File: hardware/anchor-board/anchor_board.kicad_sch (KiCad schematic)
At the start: 72 parts, among them J1 USB4105-GF-A, J2 SWD 2x5 1.27mm, J3 UART TX/RX/GND, J4 GPIO breakout, J5 3V0 current shunt, J6 LED disable, J7 Reset/boot strap, J8 TC2030 SWD, SW1 SKHHALA010, U1 DWM3001C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

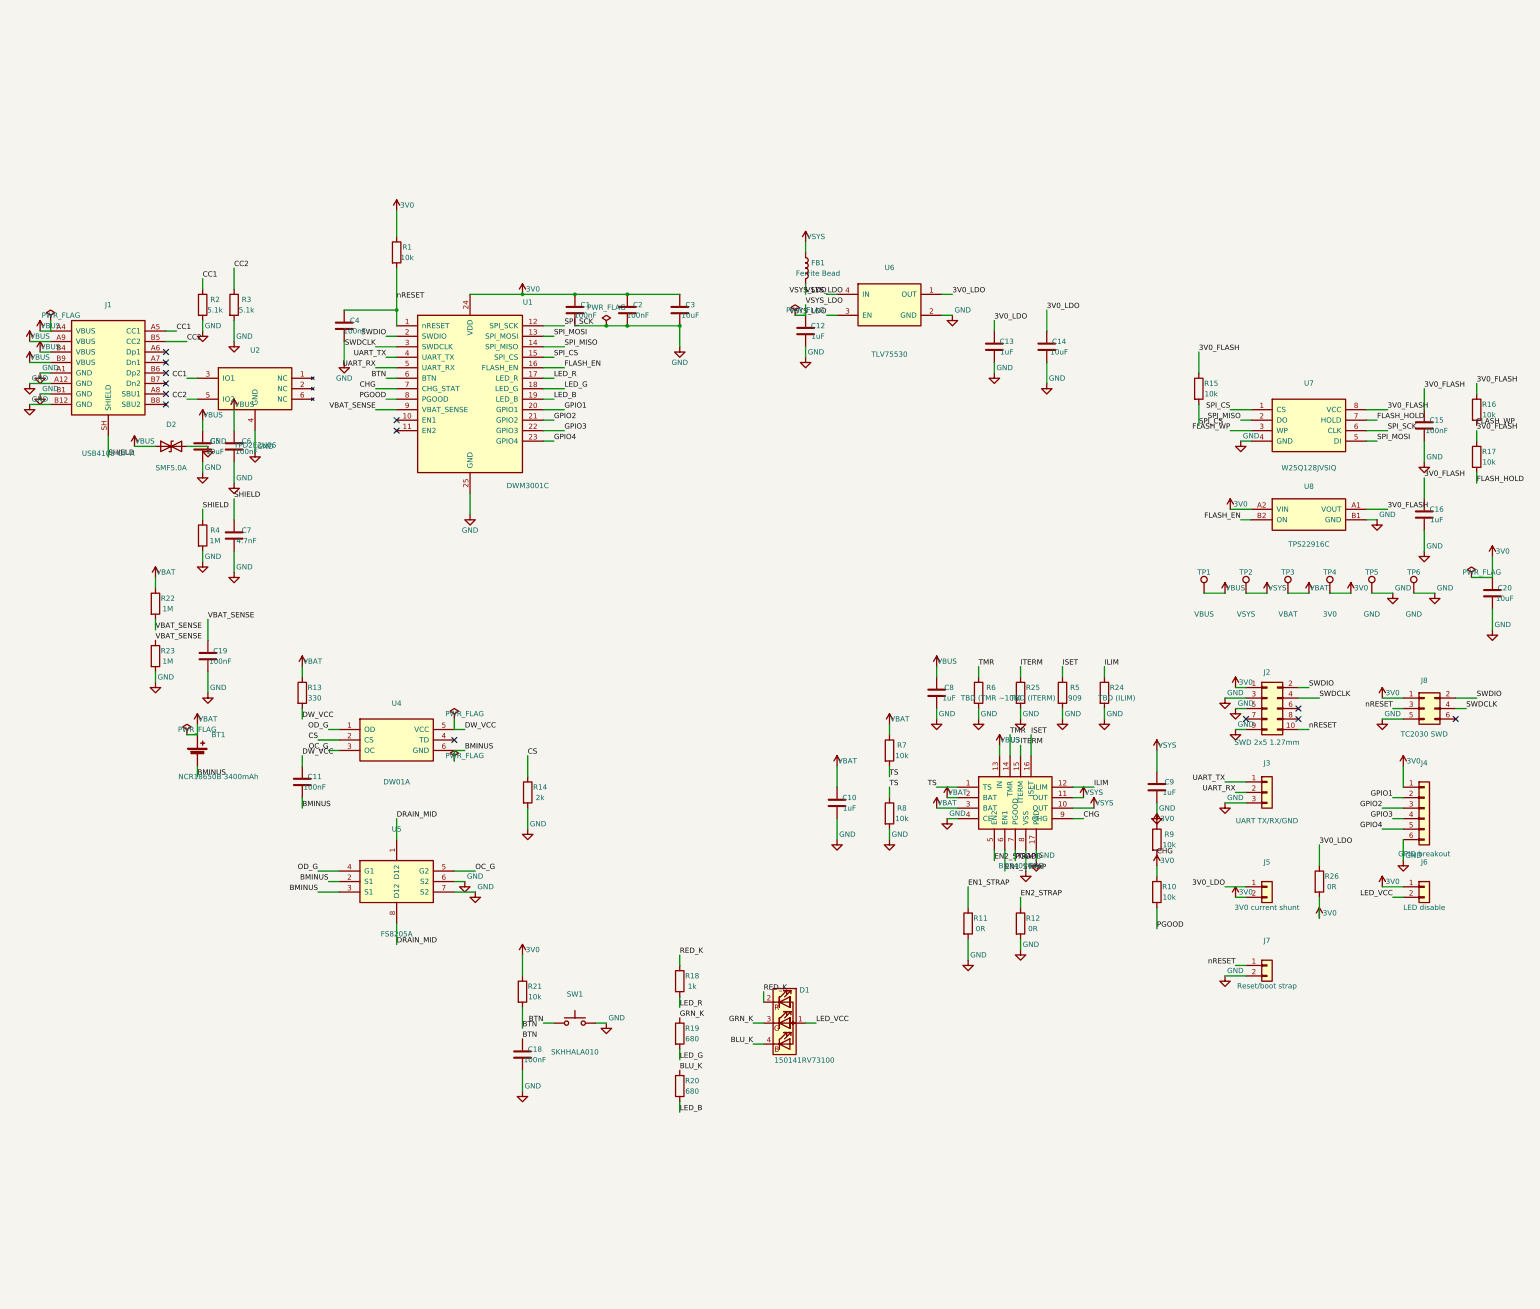
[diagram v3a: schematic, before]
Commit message: Group schematic into framed functional sections
Each block (§4.1-4.9 + §7 dev rail) is now translated as a unit into
its own region of the sheet and wrapped in a dashed frame with a
heading, instead of components being scattered across the page.

- SECTION_REFS maps every ref to its block; SECTION_TARGET gives each
  block a placement on the grid, roughly following power flow (USB-C
  top-left, rails across the top, module centre, peripherals down the
  right, dev aids along the bottom)
- blocks keep their internal relative layout — only the whole block
  moves; §4.1's hand-drawn wires/junctions/ports translate with it
- per-section frames are sized from the actual extent of each block's
  components, stubs and labels (sec_pts), drawn as a dashed polyline
  with a text heading
- ERC still 0/0

Within-block density (e.g. the charger, USB-C) is unchanged and left
for hand-tidying in KiCad.
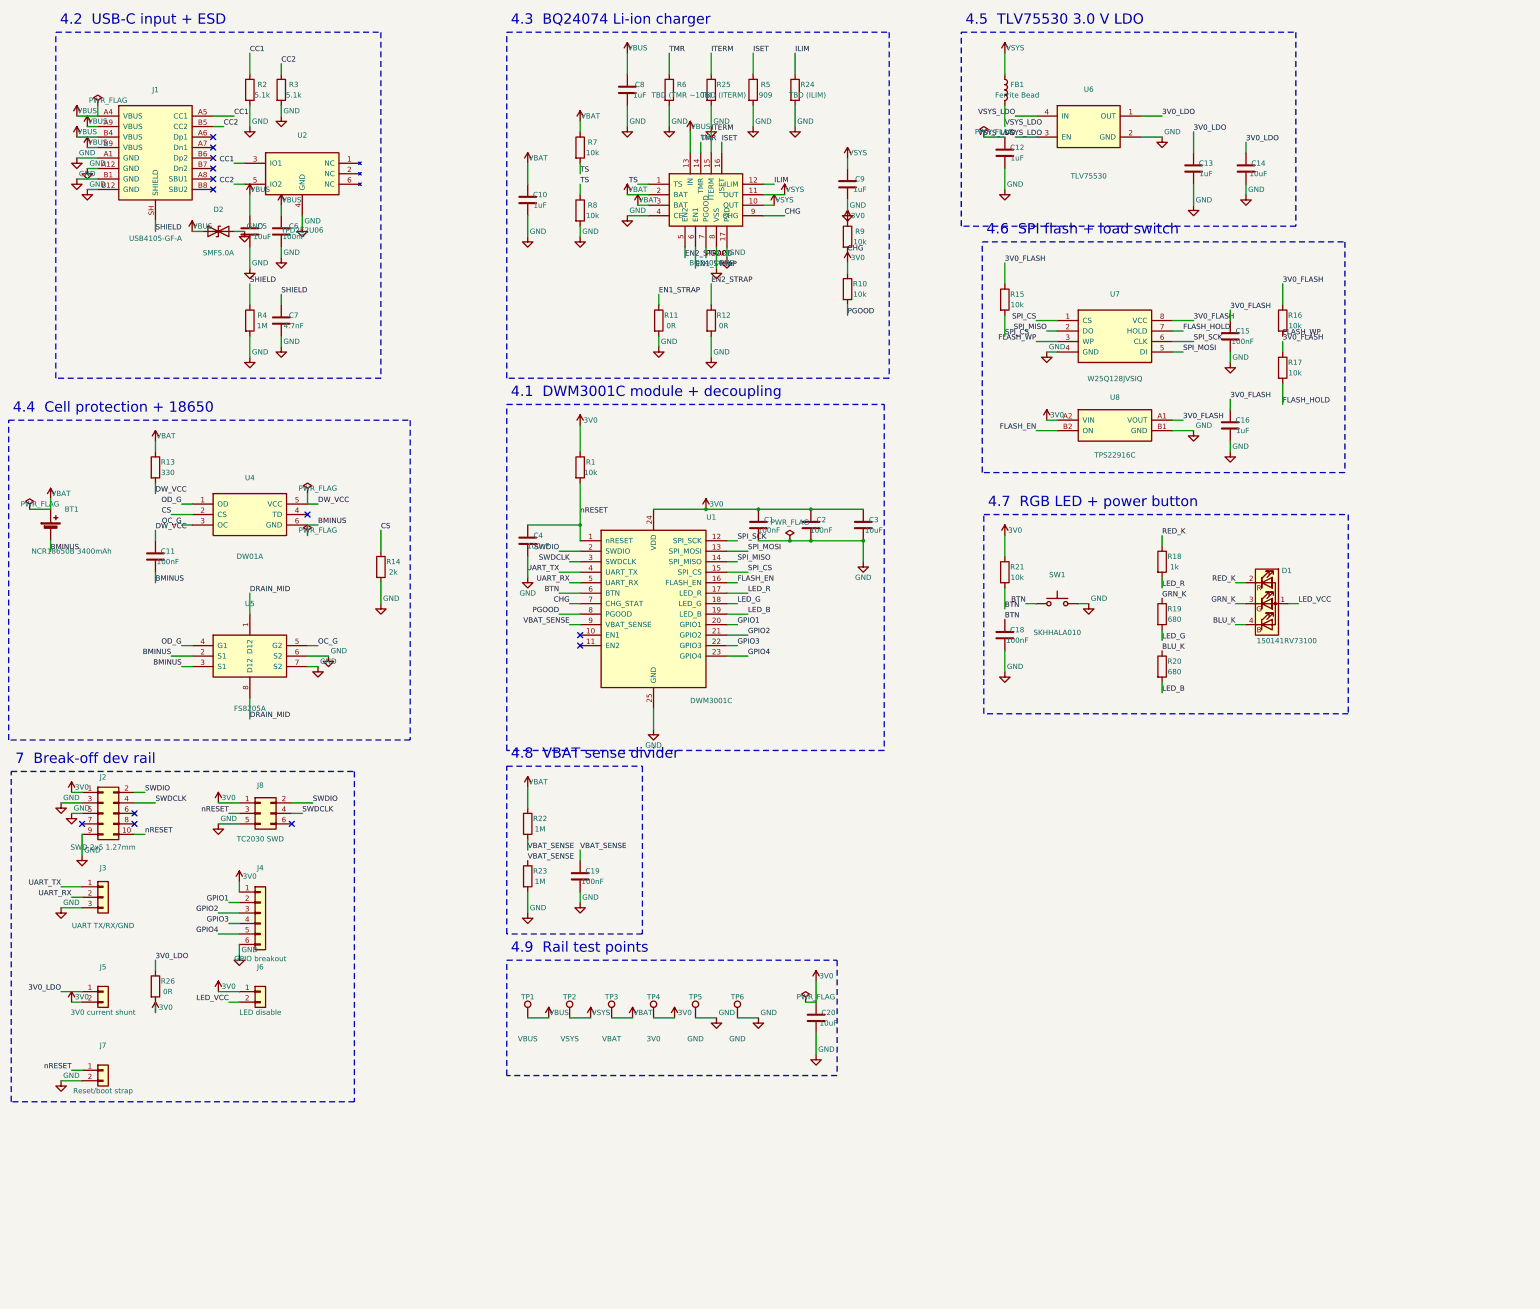
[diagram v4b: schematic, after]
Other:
- note added: "4.1 DWM3001C module + decoupling"
- note added: "4.2 USB-C input + ESD"
- note added: "4.3 BQ24074 Li-ion charger"
- note added: "4.4 Cell protection + 18650"
- note added: "4.5 TLV75530 3.0 V LDO"
- note added: "4.6 SPI flash + load switch"
- note added: "4.7 RGB LED + power button"
- note added: "4.8 VBAT sense divider"
- note added: "4.9 Rail test points"
- note added: "7 Break-off dev rail"

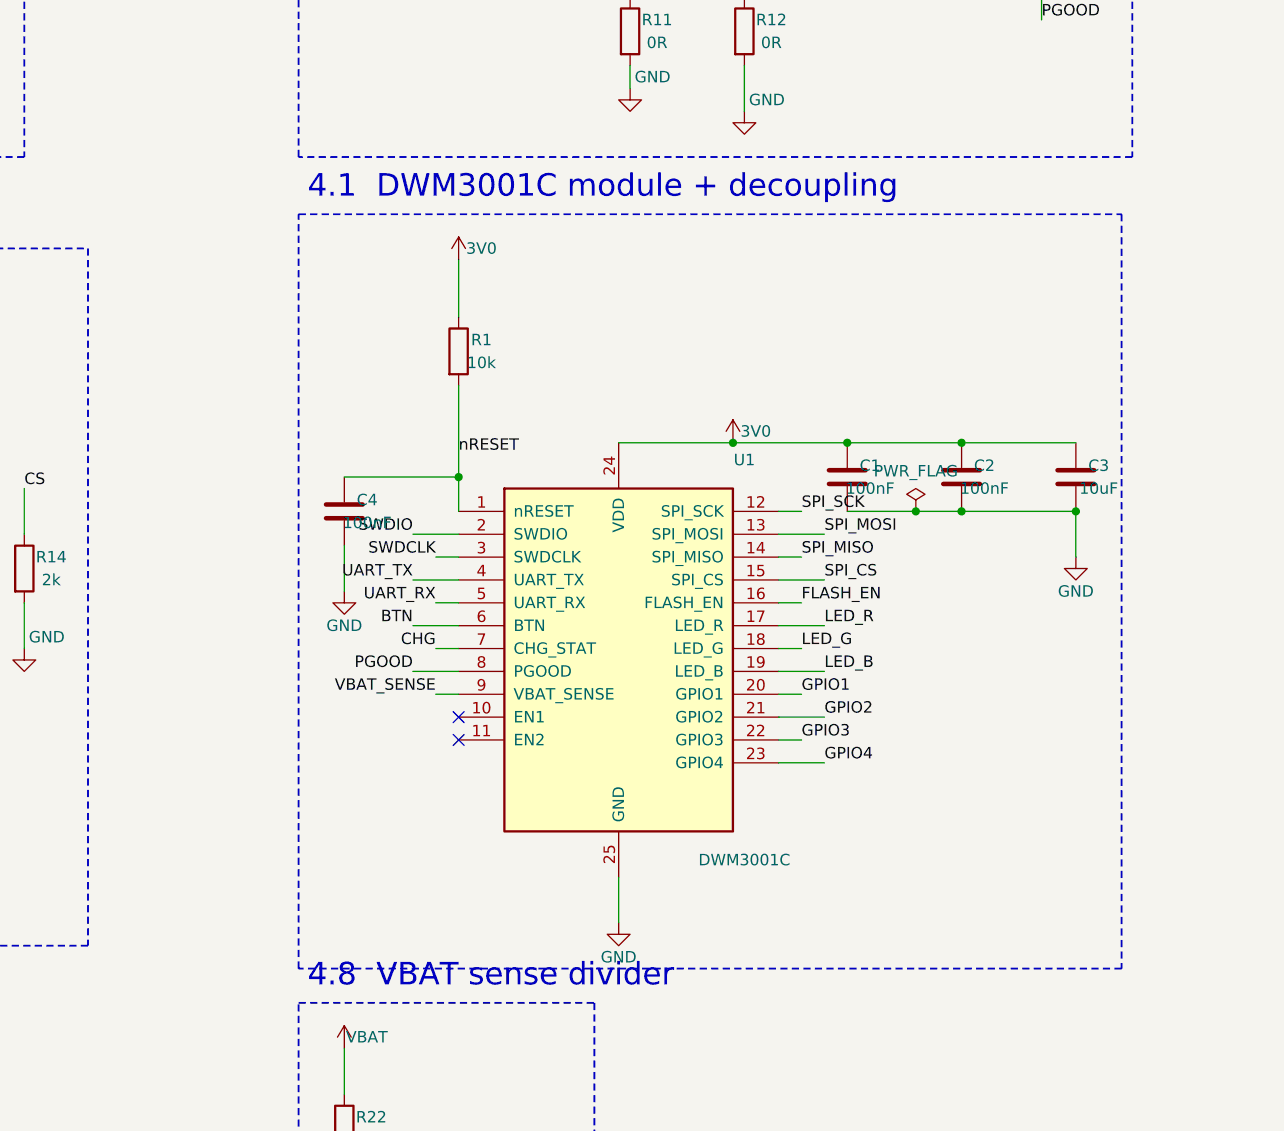
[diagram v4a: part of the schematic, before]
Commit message: Reconcile DWM3001C symbol + netlist against the real castellation map
The DWM3001C symbol was a 25-pin placeholder with sequential pin
numbers that didn't match the module. Rebuilt it as the real 48-pin
part:

- new tools/gen_dwm3001c_symbol.py generates the symbol — all 48
  castellations numbered per the datasheet (Rev F §3), used pins named
  by board function, unused pins keep their datasheet GPIO name and are
  typed no_connect (those pads float by design)
- function->GPIO assignment finalised: VBAT_SENSE on P0.31/AIN7 (ADC-
  capable), SWD/RESET on the dedicated pins, on-module accel I2C
  (P0.24/P1.04) and NFC pins (P0.09/P0.10) left NC
- gen_schematic.py: §4.1 reworked from hand-drawn wires to label/port
  connectivity like every other block; all U1 pin references remapped
  to real numbers; EN1/EN2 removed (never existed on the module — the
  BQ24074 mode is hard-strapped via R11/R12)
- added a PWR_FLAG on GND (the new symbol's grounds are all power_in)
- README §5 pin table updated from "proposed" to the reconciled map

ERC 0/0. This was the last gate before PCB layout.
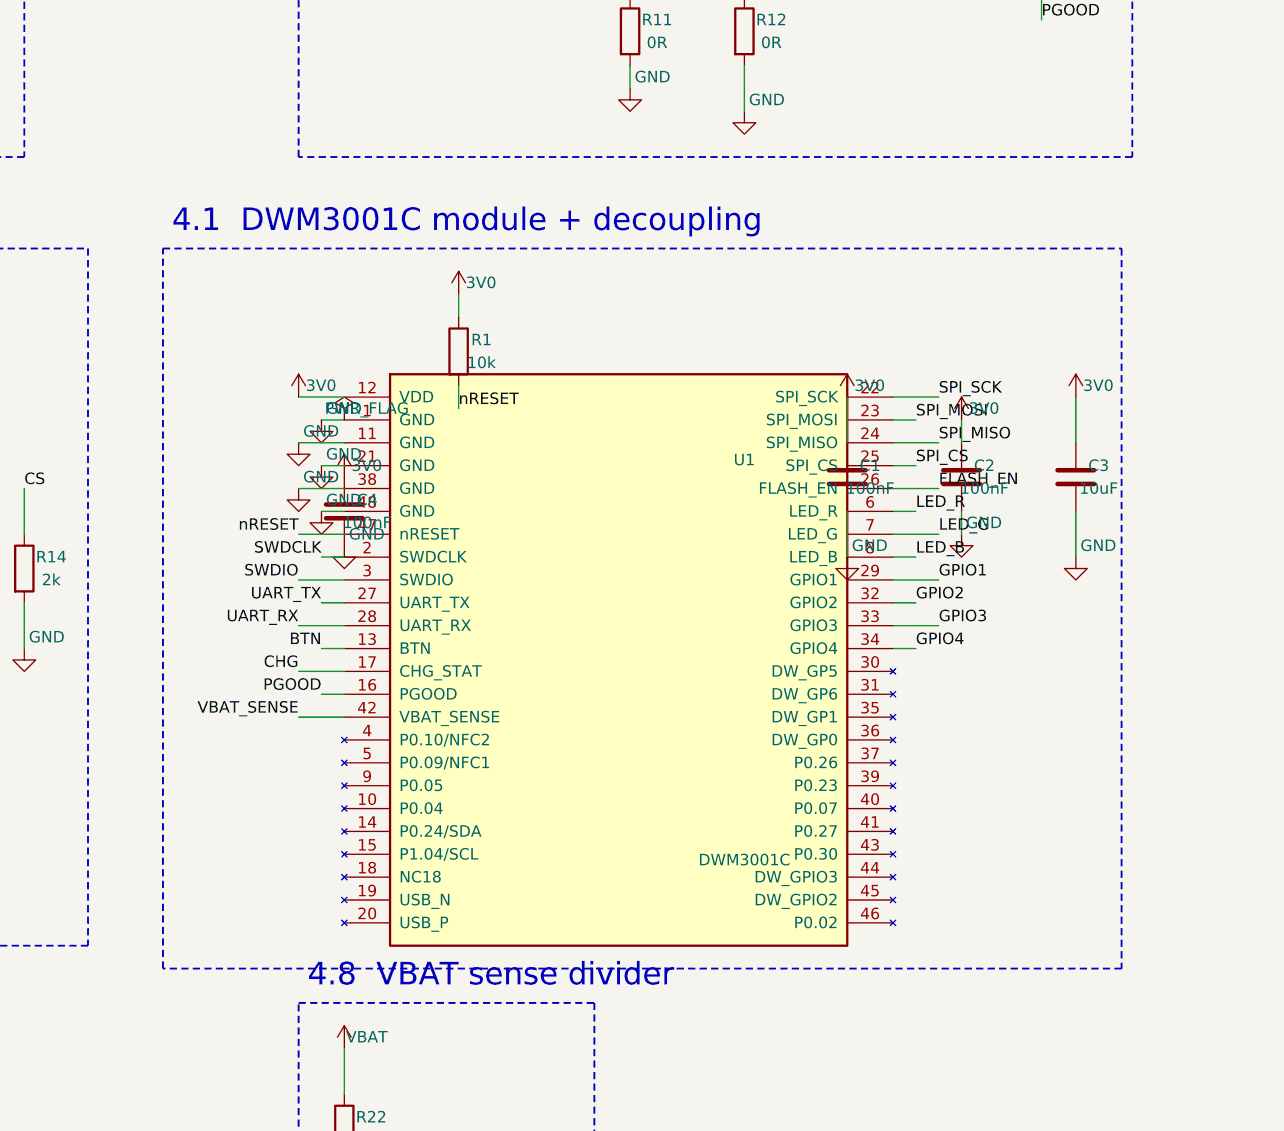
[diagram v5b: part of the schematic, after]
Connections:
- net 3V0: now also C4.1, U1.12 (VDD); no longer U1.24 (VDD)
- net BTN: now also U1.13 (BTN); no longer U1.6 (BTN)
- net CHG: now also U1.17 (CHG_STAT); no longer U1.7 (CHG_STAT)
- net FLASH_EN: now also U1.26 (FLASH_EN); no longer U1.16 (FLASH_EN)
- net GND: now also U1.1 (GND), U1.11 (GND), U1.21 (GND), U1.38 (GND), U1.48 (GND); no longer U1.25 (GND)
- net GPIO1: now also U1.29 (GPIO1); no longer U1.20 (GPIO1)
- net GPIO2: now also U1.32 (GPIO2); no longer U1.21 (GPIO2)
- net GPIO3: now also U1.33 (GPIO3); no longer U1.22 (GPIO3)
- net GPIO4: now also U1.34 (GPIO4); no longer U1.23 (GPIO4)
- net LED_B: now also U1.8 (LED_B); no longer U1.19 (LED_B)
- net LED_G: now also U1.7 (LED_G); no longer U1.18 (LED_G)
- net LED_R: now also U1.6 (LED_R); no longer U1.17 (LED_R)
- net PGOOD: now also U1.16 (PGOOD); no longer U1.8 (PGOOD)
- net SPI_CS: now also U1.25 (SPI_CS); no longer U1.15 (SPI_CS)
- net SPI_MISO: now also U1.24 (SPI_MISO); no longer U1.14 (SPI_MISO)
- net SPI_MOSI: now also U1.23 (SPI_MOSI); no longer U1.13 (SPI_MOSI)
- net SPI_SCK: now also U1.22 (SPI_SCK); no longer U1.12 (SPI_SCK)
- net SWDCLK: now also U1.2 (SWDCLK); no longer U1.3 (SWDCLK)
- net SWDIO: now also U1.3 (SWDIO); no longer U1.2 (SWDIO)
- net UART_RX: now also U1.28 (UART_RX); no longer U1.5 (UART_RX)
- net UART_TX: now also U1.27 (UART_TX); no longer U1.4 (UART_TX)
- net VBAT_SENSE: now also U1.42 (VBAT_SENSE); no longer U1.9 (VBAT_SENSE)
- net nRESET: now also U1.47 (nRESET); no longer C4.1, U1.1 (nRESET)
- no-connect marks 13 -> 11
